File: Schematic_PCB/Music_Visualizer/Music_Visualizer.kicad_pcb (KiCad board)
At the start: 2 copper layers, 295.6 x 157.9 mm, 243 parts, among them J1 AudioJack2_Ground, J2 PJ-079BH, SW1 SW_SPDT, SW2 SW_SPST, U1 LM324, U10 LM3915N-1, U11 LM3915N-1, U12 LM3915N-1, U13 LM3915N-1, U14 LM3915N-1, U15 LM3915N-1, U16 NCP161ASN350T1G, U17 NCS333ASQ3T2G, U2 LM324, U3 LM324, U4 LM324, U5 LM324, U6 LM324, U7 LT1054, U8 MC78L05_TO92, U9 LM3915N-1

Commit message: Properly traced 9V power to LEDs
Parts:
- removed C60, C61, C62, C63, C64, C65: 10u, Capacitor_THT:CP_Radial_D5.0mm_P2.00mm
- moved JP2 288.8 mm to (68.6, 139.7)
- moved C59 214.5 mm to (304.8, 148.6), turned to -90 degrees
- moved C55 9.67 mm to (317.5, 167.6)
- moved C54 9.14 mm to (313.7, 160.0)
- moved U7 7.76 mm to (321.6, 158.8)
- moved R82 7.53 mm to (334.0, 154.9), turned to 0 degrees
- moved C52 6.48 mm to (326.4, 147.3), turned to 0 degrees
- moved D71 6.47 mm to (332.7, 162.6)
- moved R73 6.23 mm to (326.4, 170.2), turned to 90 degrees
- moved C56 4.70 mm to (331.5, 169.8)
- moved R74 4.70 mm to (337.8, 169.9)
- moved C53 3.59 mm to (326.4, 151.1), turned to 0 degrees
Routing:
- net +9V: track 843.2 -> 1134.2 mm
- net Net-(D71-Pad2): track 0.00 -> 7.81 mm

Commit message: Rounded PCB corners
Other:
- board size 295.6 x 157.9 mm -> 295 x 155 mm
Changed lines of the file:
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@@
     )
   )
-  (gr_line (start 355.6 24.93) (end 60 24.93) (layer "Edge.Cuts") (width 0.1))
-  (gr_line (start 355.6 182.88) (end 355.6 24.93) (layer "Edge.Cuts") (width 0.1))
-  (gr_line (start 60 24.93) (end 60 182.88) (layer "Edge.Cuts") (width 0.1))
-  (gr_line (start 60 182.88) (end 355.6 182.88) (layer "Edge.Cuts") (width 0.1))
+  (gr_line (start 60 170) (end 60 35) (layer "Edge.Cuts") (width 0.1))
+  (gr_line (start 355 170) (end 355 35) (layer "Edge.Cuts") (width 0.1))
+  (gr_line (start 345 180) (end 75 180) (layer "Edge.Cuts") (width 0.1))
+  (gr_arc (start 70 180) (mid 62.928932 177.071068) (end 60 170) (layer "Edge.Cuts") (width 0.1))
+  (gr_line (start 70 25) (end 345 25) (layer "Edge.Cuts") (width 0.1))
+  (gr_arc (start 345 25) (mid 352.071068 27.928932) (end 355 35) (layer "Edge.Cuts") (width 0.1))
+  (gr_arc (start 60 35) (mid 62.928932 27.928932) (end 70 25) (layer "Edge.Cuts") (width 0.1))
+  (gr_arc (start 355 170) (mid 352.071068 177.071068) (end 345 180) (layer "Edge.Cuts") (width 0.1))
+  (gr_line (start 75 180) (end 70 180) (layer "Edge.Cuts") (width 0.1))
   (gr_text "Jack Source\n" (at 94.18 169.41) (layer "F.SilkS")
     (effects (font (size 1.5 1.5) (thickness 0.25)))

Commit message: Added 7th LM324 Quad-op-amp IC to Filter array, updated numbering on all other ICs
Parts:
- added U7: LM324, Package_SO:SOIC-14_3.9x8.7mm_P1.27mm, F.Cu at (331.5, 124.5)
- moved U9 66.9 mm to (276.9, 163.8)
- moved C50 66.9 mm to (275.4, 157.5)
- moved C51 66.9 mm to (276.9, 171.4)
- moved C57 20.3 mm to (221.0, 171.4)
- moved U17 20.3 mm to (215.1, 171.4)
- moved C58 20.3 mm to (209.6, 171.4)
- moved RV2 20.3 mm to (232.4, 176.3)
- moved U18 20.3 mm to (246.4, 171.4)
- renumbered U9 to U10, U10 to U11, U11 to U12, U12 to U13, U13 to U14, U14 to U15, U15 to U16, U16 to U17, U17 to U18, U7 to U8, U8 to U9
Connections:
- C21 pad 2: Net-(C21-Pad2) -> Net-(R36-Pad1)
- C24 pad 2: Net-(C24-Pad2) -> Net-(U4-Pad10)
- C27 pad 2: Net-(C27-Pad2) -> Net-(R45-Pad1)
- C33 pad 2: Net-(C33-Pad2) -> Net-(R54-Pad1)
- C37 pad 2: Net-(C37-Pad2) -> Net-(R60-Pad1)
- C7 pad 2: Net-(C7-Pad2) -> Net-(U2-Pad1)
- C8 pad 2: Net-(C8-Pad2) -> Net-(U2-Pad3)
- R11 pad 1: Net-(C7-Pad2) -> Net-(U2-Pad1)
- R11 pad 2: Net-(C8-Pad2) -> Net-(U2-Pad3)
- R12 pad 1: Net-(C7-Pad2) -> Net-(U2-Pad1)
- R14 pad 1: Net-(C7-Pad2) -> Net-(U2-Pad1)
- R35 pad 1: Net-(C21-Pad2) -> Net-(R36-Pad1)
- R36 pad 1: Net-(C21-Pad2) -> Net-(R36-Pad1)
- R38 pad 2: Net-(C24-Pad2) -> Net-(U4-Pad10)
- R44 pad 1: Net-(C27-Pad2) -> Net-(R45-Pad1)
- R45 pad 1: Net-(C27-Pad2) -> Net-(R45-Pad1)
- R53 pad 1: Net-(C33-Pad2) -> Net-(R54-Pad1)
- R54 pad 1: Net-(C33-Pad2) -> Net-(R54-Pad1)
- R59 pad 1: Net-(C37-Pad2) -> Net-(R60-Pad1)
- R60 pad 1: Net-(C37-Pad2) -> Net-(R60-Pad1)
- U1 pad 12: Net-(C8-Pad2) -> Net-(U1-Pad12)
- U1 pad 13: Net-(R12-Pad2) -> -5V
- U1 pad 14: Net-(C7-Pad2) -> Net-(U1-Pad12)
- U2 pad 1: Net-(C9-Pad2) -> Net-(U2-Pad1)
- U2 pad 10: Net-(C14-Pad2) -> Net-(C12-Pad2)
- U2 pad 12: Net-(C16-Pad2) -> Net-(U2-Pad12)
- U2 pad 13: GND -> -5V
- U2 pad 14: Net-(C15-Pad2) -> Net-(U2-Pad12)
- U2 pad 2: GND -> Net-(R12-Pad2)
- U2 pad 3: Net-(C10-Pad2) -> Net-(U2-Pad3)
- U2 pad 5: Net-(C12-Pad2) -> Net-(C10-Pad2)
- U2 pad 7: Net-(C11-Pad2) -> Net-(C9-Pad2)
- U2 pad 8: Net-(C13-Pad2) -> Net-(C11-Pad2)
- U3 pad 1: Net-(C17-Pad2) -> Net-(C13-Pad2)
- U3 pad 10: Net-(C22-Pad2) -> Net-(C18-Pad2)
- U3 pad 12: Net-(C24-Pad2) -> Net-(U3-Pad14)
- U3 pad 13: GND -> -5V
- U3 pad 14: Net-(C23-Pad2) -> Net-(U3-Pad14)
- U3 pad 3: Net-(C18-Pad2) -> Net-(C14-Pad2)
- U3 pad 5: Net-(C20-Pad2) -> Net-(C16-Pad2)
- U3 pad 6: Net-(R31-Pad2) -> GND
- U3 pad 7: Net-(C19-Pad2) -> Net-(C15-Pad2)
- U3 pad 8: Net-(C21-Pad2) -> Net-(C17-Pad2)
- U4 pad 1: Net-(C25-Pad2) -> Net-(C19-Pad2)
- U4 pad 10: Net-(C30-Pad2) -> Net-(U4-Pad10)
- U4 pad 12: Net-(C32-Pad2) -> Net-(U4-Pad12)
- U4 pad 13: GND -> -5V
- U4 pad 14: Net-(C31-Pad2) -> Net-(U4-Pad12)
- U4 pad 2: GND -> Net-(R31-Pad2)
- U4 pad 3: Net-(C26-Pad2) -> Net-(C20-Pad2)
- U4 pad 5: Net-(C28-Pad2) -> Net-(C22-Pad2)
- U4 pad 7: Net-(C27-Pad2) -> Net-(R36-Pad1)
- U4 pad 8: Net-(C29-Pad2) -> Net-(C23-Pad2)
- U5 pad 1: Net-(C33-Pad2) -> Net-(C25-Pad2)
- U5 pad 10: Net-(C38-Pad2) -> Net-(C30-Pad2)
- U5 pad 12: Net-(C40-Pad2) -> Net-(U5-Pad12)
- U5 pad 13: GND -> -5V
- U5 pad 14: Net-(C39-Pad2) -> Net-(U5-Pad12)
- U5 pad 3: Net-(C34-Pad2) -> Net-(C26-Pad2)
- U5 pad 5: Net-(C36-Pad2) -> Net-(C28-Pad2)
- U5 pad 7: Net-(C35-Pad2) -> Net-(R45-Pad1)
- U5 pad 8: Net-(C37-Pad2) -> Net-(C29-Pad2)
- U6 pad 1: Net-(C41-Pad2) -> Net-(C31-Pad2)
- U6 pad 10: Net-(U6-Pad10) -> Net-(C36-Pad2)
- U6 pad 13: Net-(U6-Pad13) -> -5V
- U6 pad 3: Net-(C42-Pad2) -> Net-(C32-Pad2)
- U6 pad 5: Net-(U6-Pad5) -> Net-(C34-Pad2)
- U6 pad 6: Net-(U6-Pad13) -> GND
- U6 pad 7: Net-(U6-Pad5) -> Net-(R54-Pad1)
- U6 pad 8: Net-(U6-Pad10) -> Net-(C35-Pad2)
- U6 pad 9: Net-(U6-Pad13) -> GND

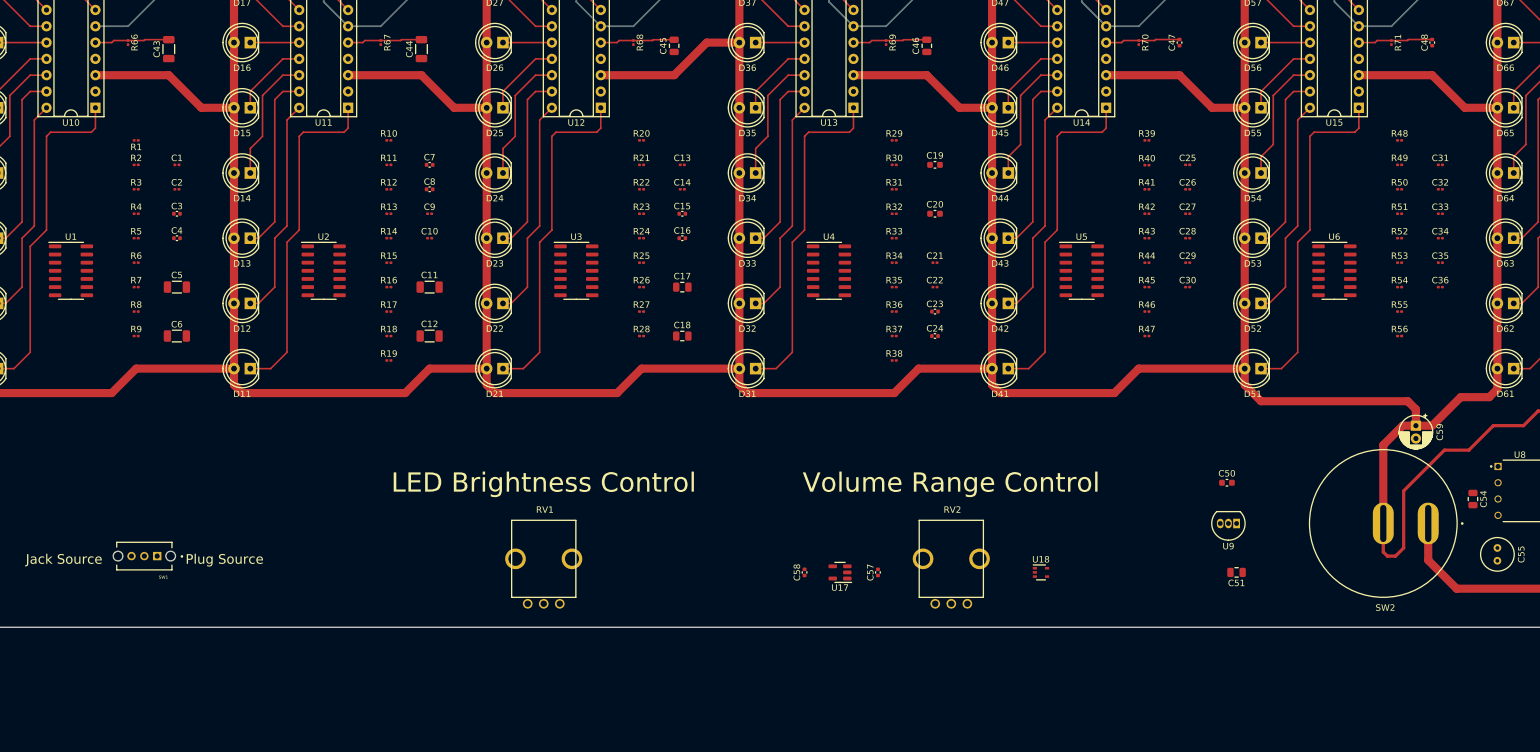
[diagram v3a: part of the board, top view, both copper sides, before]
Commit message: Routed bass and sub-bass
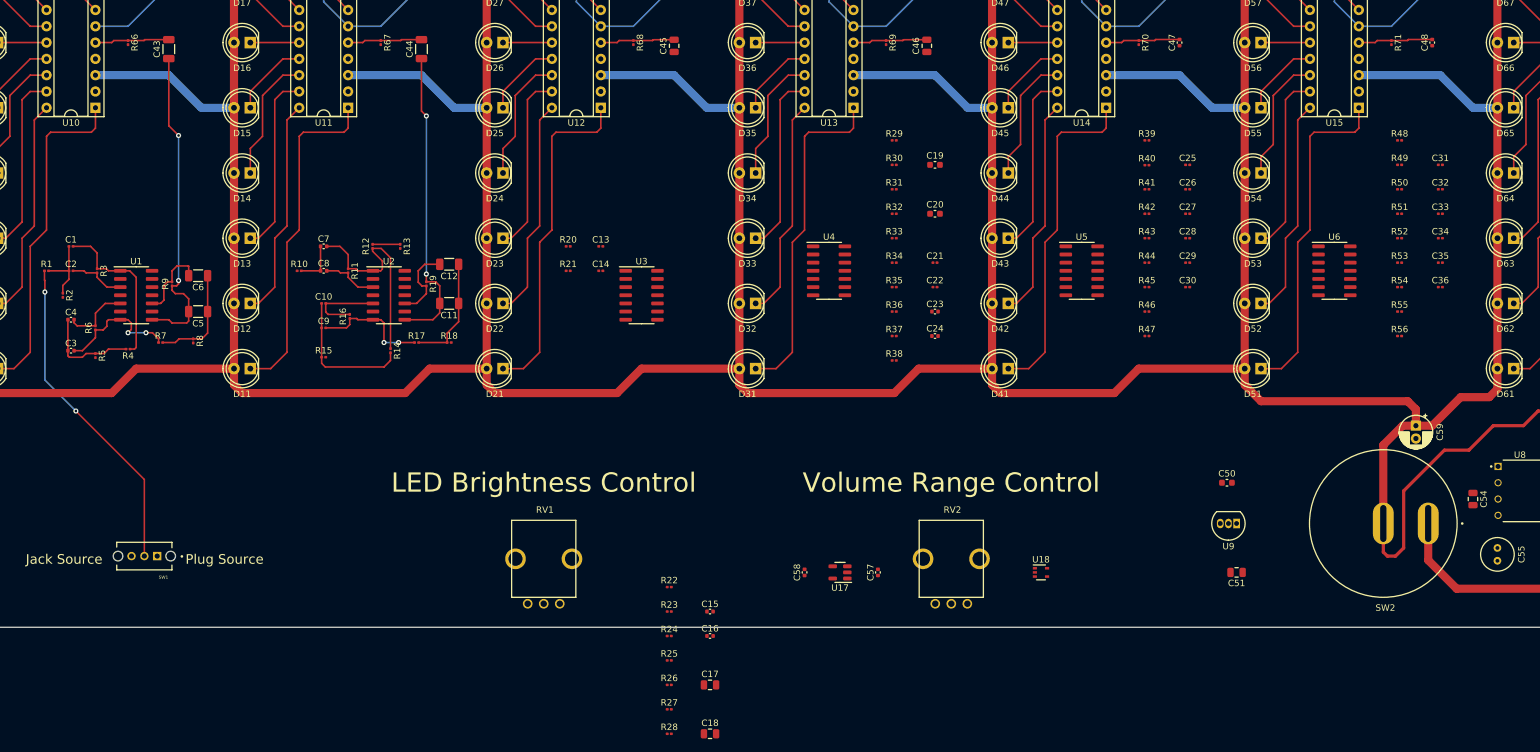
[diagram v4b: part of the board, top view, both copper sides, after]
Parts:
- moved C15 62.1 mm to (194.8, 177.5)
- moved C16 62.1 mm to (194.8, 181.4)
- moved C17 62.1 mm to (194.8, 189.0)
- moved C18 62.1 mm to (194.8, 196.6)
- moved R23 62.1 mm to (188.5, 177.5)
- moved R24 62.1 mm to (188.5, 181.4)
- moved R25 62.1 mm to (188.5, 185.2)
- moved R26 62.1 mm to (188.5, 189.0)
- moved R27 62.1 mm to (188.5, 192.8)
- moved R28 62.1 mm to (188.5, 196.6)
- moved R22 62.1 mm to (188.5, 173.7)
- moved C3 27.0 mm to (95.2, 136.9)
- moved R1 24.7 mm to (91.4, 124.5), turned to 0 degrees
- moved R10 24.7 mm to (130.8, 124.5)
- moved C9 24.3 mm to (134.6, 133.3)
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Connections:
- U1 pad 12: Net-(U1-Pad12) -> unconnected-(U1-Pad12)
- U1 pad 13: -5V -> unconnected-(U1-Pad13)
- U1 pad 14: Net-(U1-Pad12) -> unconnected-(U1-Pad14)
- U2 pad 12: Net-(U2-Pad12) -> unconnected-(U2-Pad12)
- U2 pad 13: -5V -> unconnected-(U2-Pad13)
- U2 pad 14: Net-(U2-Pad12) -> unconnected-(U2-Pad14)
- U3 pad 12: Net-(U3-Pad14) -> unconnected-(U3-Pad12)
- U3 pad 13: -5V -> unconnected-(U3-Pad13)
- U3 pad 14: Net-(U3-Pad14) -> unconnected-(U3-Pad14)
- U4 pad 12: Net-(U4-Pad12) -> unconnected-(U4-Pad12)
- U4 pad 13: -5V -> unconnected-(U4-Pad13)
- U4 pad 14: Net-(U4-Pad12) -> unconnected-(U4-Pad14)
- U5 pad 12: Net-(U5-Pad12) -> unconnected-(U5-Pad12)
- U5 pad 13: -5V -> unconnected-(U5-Pad13)
- U5 pad 14: Net-(U5-Pad12) -> unconnected-(U5-Pad14)
- U6 pad 12: Net-(U6-Pad12) -> unconnected-(U6-Pad12)
- U6 pad 13: -5V -> unconnected-(U6-Pad13)
- U6 pad 14: Net-(U6-Pad12) -> unconnected-(U6-Pad14)
- U7 pad 11: (no net) -> -5V
- U7 pad 12: Net-(U7-Pad12) -> unconnected-(U7-Pad12)
- U7 pad 13: -5V -> unconnected-(U7-Pad13)
- U7 pad 14: Net-(U7-Pad12) -> unconnected-(U7-Pad14)
- U7 pad 4: (no net) -> +5V
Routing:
- net Vsig: track 0.00 -> 50.9 mm, vias 0 -> 2
- net Net-(C43-Pad1): track 0.00 -> 50.2 mm, vias 0 -> 2
- net Net-(C11-Pad2): track 0.00 -> 47.5 mm, vias 0 -> 2
- net Net-(U2-Pad1): track 0.00 -> 33.1 mm
- net Net-(C1-Pad2): track 0.00 -> 25.3 mm
- net Net-(C10-Pad1): track 0.00 -> 21.9 mm
- net Net-(C3-Pad2): track 0.00 -> 19.7 mm, vias 0 -> 2
- net Net-(C9-Pad2): track 0.00 -> 18.3 mm, vias 0 -> 2
- net Net-(C11-Pad1): track 0.00 -> 17.4 mm
- net Net-(C5-Pad1): track 0.00 -> 16.6 mm
- net Net-(C3-Pad1): track 0.00 -> 15.3 mm
- net Net-(C10-Pad2): track 0.00 -> 12.6 mm
- net Net-(C12-Pad2): track 0.00 -> 12.3 mm
- net Net-(C6-Pad2): track 0.00 -> 12.0 mm
- net Net-(C1-Pad1): track 0.00 -> 10.9 mm
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
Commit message: Added ground pour to top and bottom layers
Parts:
- moved C17 68.3 mm to (193.0, 120.7)
- moved C18 68.3 mm to (193.0, 128.3)
- moved C15 49.4 mm to (172.7, 133.3)
- moved C16 49.4 mm to (172.7, 137.2)
- moved R20 4.58 mm to (170.2, 124.5)
- moved R21 3.81 mm to (172.7, 128.3)
- moved C13 3.81 mm to (174.0, 120.7)
- moved C14 3.81 mm to (174.0, 124.5)
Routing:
- net Net-(R12-Pad2): track 4.32 -> 13.9 mm, vias 0 -> 2
- net GND: vias 0 -> 1
- added copper zone on B.Cu, net GND
- added copper zone on F.Cu, net GND
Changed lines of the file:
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@@
   )
   (footprint "Capacitor_SMD:C_0201_0603Metric" (layer "F.Cu")
-    (at 177.8 124.46)
+    (at 173.99 124.46)
     (descr "Capacitor SMD 0201 (0603 Metric), square (rectangular) end terminal, IPC_7351 nominal, (Body size source: https://www.vishay.com/docs/20052/crcw0201e3.pdf), generated with kicad-footprint-generator")
     (tags "capacitor")
@@
   )
   (footprint "Resistor_SMD:R_0201_0603Metric" (layer "F.Cu")
-    (at 172.72 120.65)
+    (at 170.18 124.46)
     (descr "Resistor SMD 0201 (0603 Metric), square (rectangular) end terminal, IPC_7351 nominal, (Body size source: https://www.vishay.com/docs/20052/crcw0201e3.pdf), generated with kicad-footprint-generator")
     (tags "resistor")
@@
   )
   (footprint "Capacitor_SMD:C_0805_2012Metric" (layer "F.Cu")
-    (at 194.818 196.596)
+    (at 193.04 128.27)
     (descr "Capacitor SMD 0805 (2012 Metric), square (rectangular) end terminal, IPC_7351 nominal, (Body size source: IPC-SM-782 page 76, https://www.pcb-3d.com/wordpress/wp-content/uploads/ipc-sm-782a_amendment_1_and_2.pdf, https://docs.google.com/spreadsheets/d/1BsfQQcO9C6DZCsRaXUlFlo91Tg2WpOkGARC1WS5S8t0/edit?usp=sharing), generated with kicad-footprint-generator")
     (tags "capacitor")
@@
   )
   (footprint "Capacitor_SMD:C_0402_1005Metric" (layer "F.Cu")
-    (at 194.818 177.546)
+    (at 172.72 133.35)
     (descr "Capacitor SMD 0402 (1005 Metric), square (rectangular) end terminal, IPC_7351 nominal, (Body size source: IPC-SM-782 page 76, https://www.pcb-3d.com/wordpress/wp-content/uploads/ipc-sm-782a_amendment_1_and_2.pdf), generated with kicad-footprint-generator")
     (tags "capacitor")
@@
   )
   (footprint "Capacitor_SMD:C_0201_0603Metric" (layer "F.Cu")
-    (at 177.8 120.65)
+    (at 173.99 120.65)
     (descr "Capacitor SMD 0201 (0603 Metric), square (rectangular) end terminal, IPC_7351 nominal, (Body size source: https://www.vishay.com/docs/20052/crcw0201e3.pdf), generated with kicad-footprint-generator")
     (tags "capacitor")
@@
   )
   (footprint "Capacitor_SMD:C_0805_2012Metric" (layer "F.Cu")
-    (at 194.818 188.976)
+    (at 193.04 120.65)
     (descr "Capacitor SMD 0805 (2012 Metric), square (rectangular) end terminal, IPC_7351 nominal, (Body size source: IPC-SM-782 page 76, https://www.pcb-3d.com/wordpress/wp-content/uploads/ipc-sm-782a_amendment_1_and_2.pdf, https://docs.google.com/spreadsheets/d/1BsfQQcO9C6DZCsRaXUlFlo91Tg2WpOkGARC1WS5S8t0/edit?usp=sharing), generated with kicad-footprint-generator")
     (tags "capacitor")
@@
   )
   (footprint "Capacitor_SMD:C_0402_1005Metric" (layer "F.Cu")
-    (at 194.818 181.356)
+    (at 172.72 137.16)
     (descr "Capacitor SMD 0402 (1005 Metric), square (rectangular) end terminal, IPC_7351 nominal, (Body size source: IPC-SM-782 page 76, https://www.pcb-3d.com/wordpress/wp-content/uploads/ipc-sm-782a_amendment_1_and_2.pdf), generated with kicad-footprint-generator")
     (tags "capacitor")
@@
   )
   (footprint "Resistor_SMD:R_0201_0603Metric" (layer "F.Cu")
-    (at 172.72 124.46)
+    (at 172.72 128.27)
     (descr "Resistor SMD 0201 (0603 Metric), square (rectangular) end terminal, IPC_7351 nominal, (Body size source: https://www.vishay.com/docs/20052/crcw0201e3.pdf), generated with kicad-footprint-generator")
     (tags "resistor")
@@
   (segment (start 134.14 124.46) (end 131.13 124.46) (width 0.254) (layer "F.Cu") (net 10))
   (segment (start 134.14 120.65) (end 134.14 124.46) (width 0.254) (layer "F.Cu") (net 10))
+  (segment (start 138.872 124.14) (end 139.192 124.46) (width 0.25) (layer "F.Cu") (net 11))
   (segment (start 142.24 120.97) (end 142.24 121.412) (width 0.25) (layer "F.Cu") (net 11))
-  (segment (start 139.634 124.14) (end 139.954 124.46) (width 0.25) (layer "F.Cu") (net 11))
   (segment (start 142.24 121.412) (end 143.764 122.936) (width 0.25) (layer "F.Cu") (net 11))
   (segment (start 135.1 120.65) (end 137.16 120.65) (width 0.25) (layer "F.Cu") (net 11))
   (segment (start 143.764 124.206) (end 143.51 124.46) (width 0.25) (layer "F.Cu") (net 11))
   (segment (start 145.034 136.586) (end 145.034 122.428) (width 0.25) (layer "F.Cu") (net 11))
+  (segment (start 138.43 124.14) (end 138.872 124.14) (width 0.25) (layer "F.Cu") (net 11))
   (segment (start 138.43 121.92) (end 138.43 124.14) (width 0.25) (layer "F.Cu") (net 11))
   (segment (start 143.576 120.97) (end 142.24 120.97) (width 0.25) (layer "F.Cu") (net 11))
-  (segment (start 139.954 124.46) (end 142.305 124.46) (width 0.25) (layer "F.Cu") (net 11))
   (segment (start 143.51 124.46) (end 142.305 124.46) (width 0.25) (layer "F.Cu") (net 11))
-  (segment (start 138.43 124.14) (end 139.634 124.14) (width 0.25) (layer "F.Cu") (net 11))
   (segment (start 145.034 122.428) (end 143.576 120.97) (width 0.25) (layer "F.Cu") (net 11))
   (segment (start 137.16 120.65) (end 138.43 121.92) (width 0.25) (layer "F.Cu") (net 11))
+  (segment (start 139.192 124.46) (end 142.305 124.46) (width 0.25) (layer "F.Cu") (net 11))
   (segment (start 143.764 122.936) (end 143.764 124.206) (width 0.25) (layer "F.Cu") (net 11))
   (segment (start 138.43 125.476) (end 139.954 127) (width 0.25) (layer "F.Cu") (net 12))
@@
   (segment (start 110.49 93.98) (end 115.57 99.06) (width 1.27) (layer "B.Cu") (net 71))
   (segment (start 102.935 125.73) (end 102.87 125.73) (width 0.25) (layer "F.Cu") (net 72))
+  (via (at 100.9142 130.81) (size 0.8) (drill 0.4) (layers "F.Cu" "B.Cu") (net 72))
   (segment (start 99.06 99.06) (end 99.06 102.235) (width 0.254) (layer "F.Cu") (net 78))
   (segment (start 86.36 139.7) (end 83.82 139.7) (width 0.254) (layer "F.Cu") (net 78))
@@
   (segment (start 96.012 146.304) (end 91.186 141.478) (width 0.25) (layer "B.Cu") (net 151))
   (segment (start 91.186 141.478) (end 91.186 127.762) (width 0.25) (layer "B.Cu") (net 151))
+  (segment (start 139.954 125.73) (end 142.305 125.73) (width 0.254) (layer "F.Cu") (net 152))
+  (segment (start 140.782 120.33) (end 140.716 120.396) (width 0.254) (layer "F.Cu") (net 152))
+  (segment (start 140.716 120.396) (end 139.954 121.158) (width 0.254) (layer "F.Cu") (net 152))
   (segment (start 142.24 120.33) (end 146.558 120.33) (width 0.254) (layer "F.Cu") (net 152))
+  (segment (start 142.24 120.33) (end 140.782 120.33) (width 0.254) (layer "F.Cu") (net 152))
+  (segment (start 139.954 121.158) (end 139.954 123.19) (width 0.254) (layer "F.Cu") (net 152))
+  (via (at 139.954 123.19) (size 0.8) (drill 0.4) (layers "F.Cu" "B.Cu") (net 152))
+  (via (at 139.954 125.73) (size 0.8) (drill 0.4) (layers "F.Cu" "B.Cu") (net 152))
+  (segment (start 139.954 123.19) (end 139.954 125.73) (width 0.254) (layer "B.Cu") (net 152))
   (segment (start 96.965 75.755) (end 96.52 76.2) (width 0.254) (layer "F.Cu") (net 155))
   (segment (start 104.14 75.755) (end 96.965 75.755) (width 0.254) (layer "F.Cu") (net 155))
@@
   (segment (start 143.51 86.36) (end 158.75 71.12) (width 0.254) (layer "B.Cu") (net 166))
   (segment (start 119.38 71.12) (end 132.08 71.12) (width 0.254) (layer "B.Cu") (net 166))
+  (zone (net 72) (net_name "GND") (layers F&B.Cu) (hatch edge 0.508)
+    (connect_pads (clearance 0.508))
+    (min_thickness 0.254) (filled_areas_thickness no)
+    (fill yes (thermal_gap 0.508) (thermal_bridge_width 0.508))
+    (polygon
+      (pts
+        (xy 355 180)
+        (xy 60 180)
+        (xy 60 25)
+        (xy 355 25)
+      )
+    )
+  )
 )
